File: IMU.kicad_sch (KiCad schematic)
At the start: 7 parts

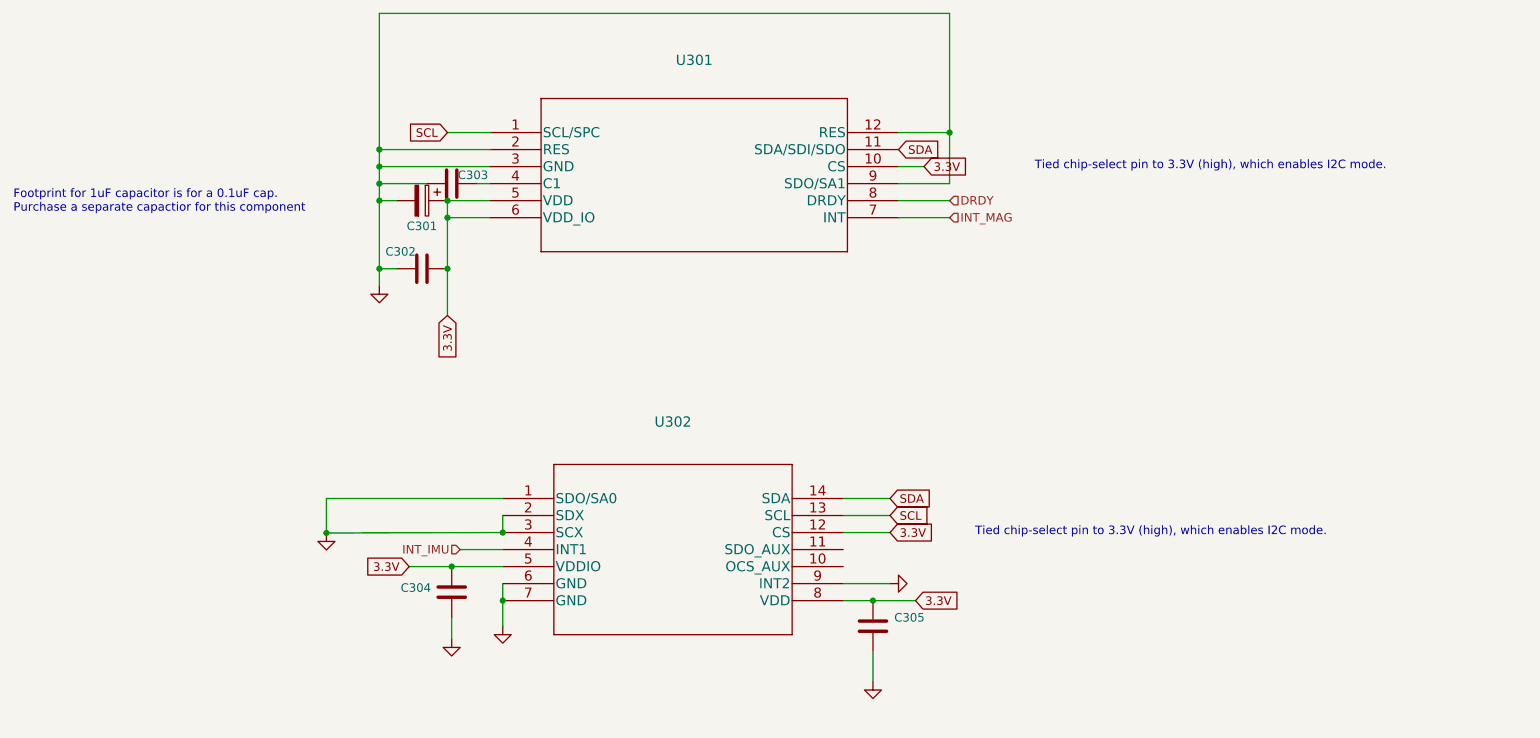
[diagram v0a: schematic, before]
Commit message: updates to schematics layout
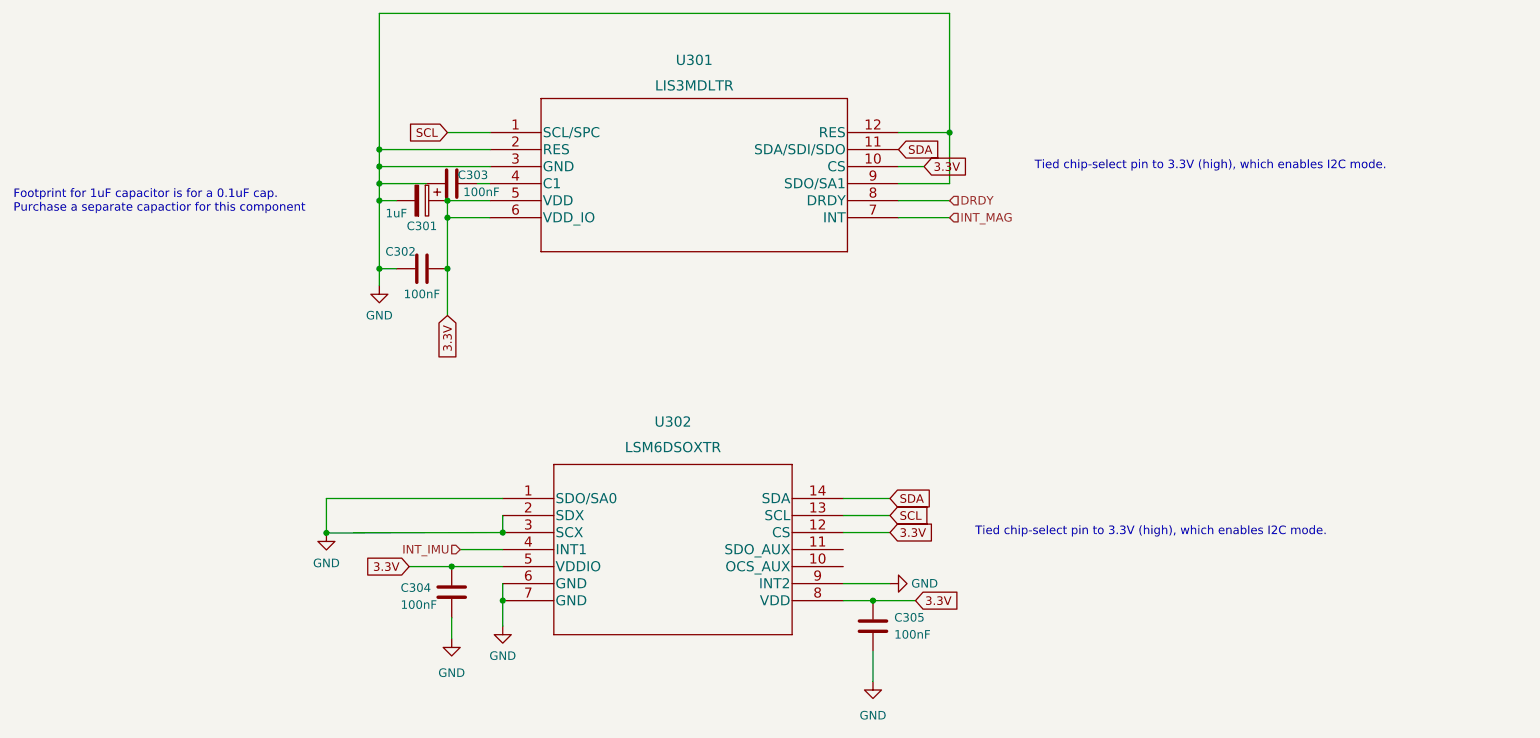
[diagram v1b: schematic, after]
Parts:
- C301: value (none) -> 1uF; footprint (none) -> 0.1uF P_Cap:UWP1H0R1MCL1GB
- C302, C303, C304, C305: value (none) -> 100nF; footprint (none) -> Capacitor_SMD:C_0603_1608Metric_Pad1.08x0.95mm_HandSolder
- U301: value (none) -> LIS3MDLTR; footprint (none) -> 3-axis magnetometer:LIS3MDLTR
- U302: value (none) -> LSM6DSOXTR; footprint (none) -> 6-axis IMU:LSM6DSOXTR
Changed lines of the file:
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@@
     (in_bom yes) (on_board yes)
     (property "Reference" "C303" (id 0) (at 100.965 74.295 90))
-    (property "Value" "" (id 1) (at 102.235 76.835 90))
-    (property "Footprint" "" (id 2) (at 101.6 74.5998 0)
+    (property "Value" "100nF" (id 1) (at 102.235 76.835 90))
+    (property "Footprint" "Capacitor_SMD:C_0603_1608Metric_Pad1.08x0.95mm_HandSolder" (id 2) (at 101.6 74.5998 0)
       (effects (font (size 1.27 1.27)) hide)
     )
@@
       (effects (font (size 1.27 1.27)) (justify left))
     )
-    (property "Value" "" (id 1) (at 163.83 142.8749 0)
-      (effects (font (size 1.27 1.27)) (justify left))
-    )
-    (property "Footprint" "" (id 2) (at 161.6202 145.415 0)
+    (property "Value" "100nF" (id 1) (at 163.83 142.8749 0)
+      (effects (font (size 1.27 1.27)) (justify left))
+    )
+    (property "Footprint" "Capacitor_SMD:C_0603_1608Metric_Pad1.08x0.95mm_HandSolder" (id 2) (at 161.6202 145.415 0)
       (effects (font (size 1.27 1.27)) hide)
     )
@@
       (effects (font (size 1.27 1.27)) hide)
     )
-    (property "Value" "" (id 1) (at 79.0951 132.2169 0))
+    (property "Value" "GND" (id 1) (at 79.0951 132.2169 0))
     (property "Footprint" "" (id 2) (at 79.0951 127.6916 0)
       (effects (font (size 1.27 1.27)) hide)
@@
       (effects (font (size 1.27 1.27)) hide)
     )
-    (property "Value" "" (id 1) (at 97.79 148.59 0))
+    (property "Value" "GND" (id 1) (at 97.79 148.59 0))
     (property "Footprint" "" (id 2) (at 97.79 143.51 0)
       (effects (font (size 1.27 1.27)) hide)
@@
       (effects (font (size 1.27 1.27)) (justify left))
     )
-    (property "Value" "" (id 1) (at 90.17 138.43 0)
-      (effects (font (size 1.27 1.27)) (justify left))
-    )
-    (property "Footprint" "" (id 2) (at 98.7552 140.335 0)
+    (property "Value" "100nF" (id 1) (at 90.17 138.43 0)
+      (effects (font (size 1.27 1.27)) (justify left))
+    )
+    (property "Footprint" "Capacitor_SMD:C_0603_1608Metric_Pad1.08x0.95mm_HandSolder" (id 2) (at 98.7552 140.335 0)
       (effects (font (size 1.27 1.27)) hide)
     )
@@
       (effects (font (size 1.524 1.524)))
     )
-    (property "Value" "" (id 1) (at 133.985 60.96 0)
-      (effects (font (size 1.524 1.524)))
-    )
-    (property "Footprint" "" (id 2) (at 133.985 61.849 0)
+    (property "Value" "LIS3MDLTR" (id 1) (at 133.985 60.96 0)
+      (effects (font (size 1.524 1.524)))
+    )
+    (property "Footprint" "3-axis magnetometer:LIS3MDLTR" (id 2) (at 133.985 61.849 0)
       (effects (font (size 1.524 1.524)) hide)
     )
@@
       (effects (font (size 1.524 1.524)))
     )
-    (property "Value" "" (id 1) (at 130.81 114.935 0)
-      (effects (font (size 1.524 1.524)))
-    )
-    (property "Footprint" "" (id 2) (at 130.81 116.459 0)
+    (property "Value" "LSM6DSOXTR" (id 1) (at 130.81 114.935 0)
+      (effects (font (size 1.524 1.524)))
+    )
+    (property "Footprint" "6-axis IMU:LSM6DSOXTR" (id 2) (at 130.81 116.459 0)
       (effects (font (size 1.524 1.524)) hide)
     )
@@
     (in_bom yes) (on_board yes)
     (property "Reference" "C301" (id 0) (at 93.345 81.915 90))
-    (property "Value" "" (id 1) (at 89.535 80.01 90))
-    (property "Footprint" "" (id 2) (at 89.535 79.0702 0)
+    (property "Value" "1uF" (id 1) (at 89.535 80.01 90))
+    (property "Footprint" "0.1uF P_Cap:UWP1H0R1MCL1GB" (id 2) (at 89.535 79.0702 0)
       (effects (font (size 1.27 1.27)) hide)
     )
@@
       (effects (font (size 1.27 1.27)) hide)
     )
-    (property "Value" "" (id 1) (at 166.37 135.2549 90)
+    (property "Value" "GND" (id 1) (at 166.37 135.2549 90)
       (effects (font (size 1.27 1.27)) (justify right))
     )
@@
       (effects (font (size 1.27 1.27)) hide)
     )
-    (property "Value" "" (id 1) (at 105.41 146.05 0))
+    (property "Value" "GND" (id 1) (at 105.41 146.05 0))
     (property "Footprint" "" (id 2) (at 105.41 141.605 0)
       (effects (font (size 1.27 1.27)) hide)
@@
       (effects (font (size 1.27 1.27)) hide)
     )
-    (property "Value" "" (id 1) (at 160.655 154.94 0))
+    (property "Value" "GND" (id 1) (at 160.655 154.94 0))
     (property "Footprint" "" (id 2) (at 160.655 149.86 0)
       (effects (font (size 1.27 1.27)) hide)
@@
       (effects (font (size 1.27 1.27)) hide)
     )
-    (property "Value" "" (id 1) (at 86.995 95.25 0))
+    (property "Value" "GND" (id 1) (at 86.995 95.25 0))
     (property "Footprint" "" (id 2) (at 86.995 90.805 0)
       (effects (font (size 1.27 1.27)) hide)
@@
     (in_bom yes) (on_board yes)
     (property "Reference" "C302" (id 0) (at 90.17 85.725 90))
-    (property "Value" "" (id 1) (at 93.345 92.075 90))
-    (property "Footprint" "" (id 2) (at 89.535 89.2302 0)
-      (effects (font (size 1.27 1.27)) hide)
-    )
+    (property "Value" "100nF" (id 1) (at 93.345 92.075 90))
+    (property "Footprint" "Capacitor_SMD:C_0603_1608Metric_Pad1.08x0.95mm_HandSolder" (id 2) (at 89.535 89.2302 0)
+      (effects (font (size 1.27 1.27)) hide)
+    )
